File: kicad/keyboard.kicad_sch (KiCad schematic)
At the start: 64 parts

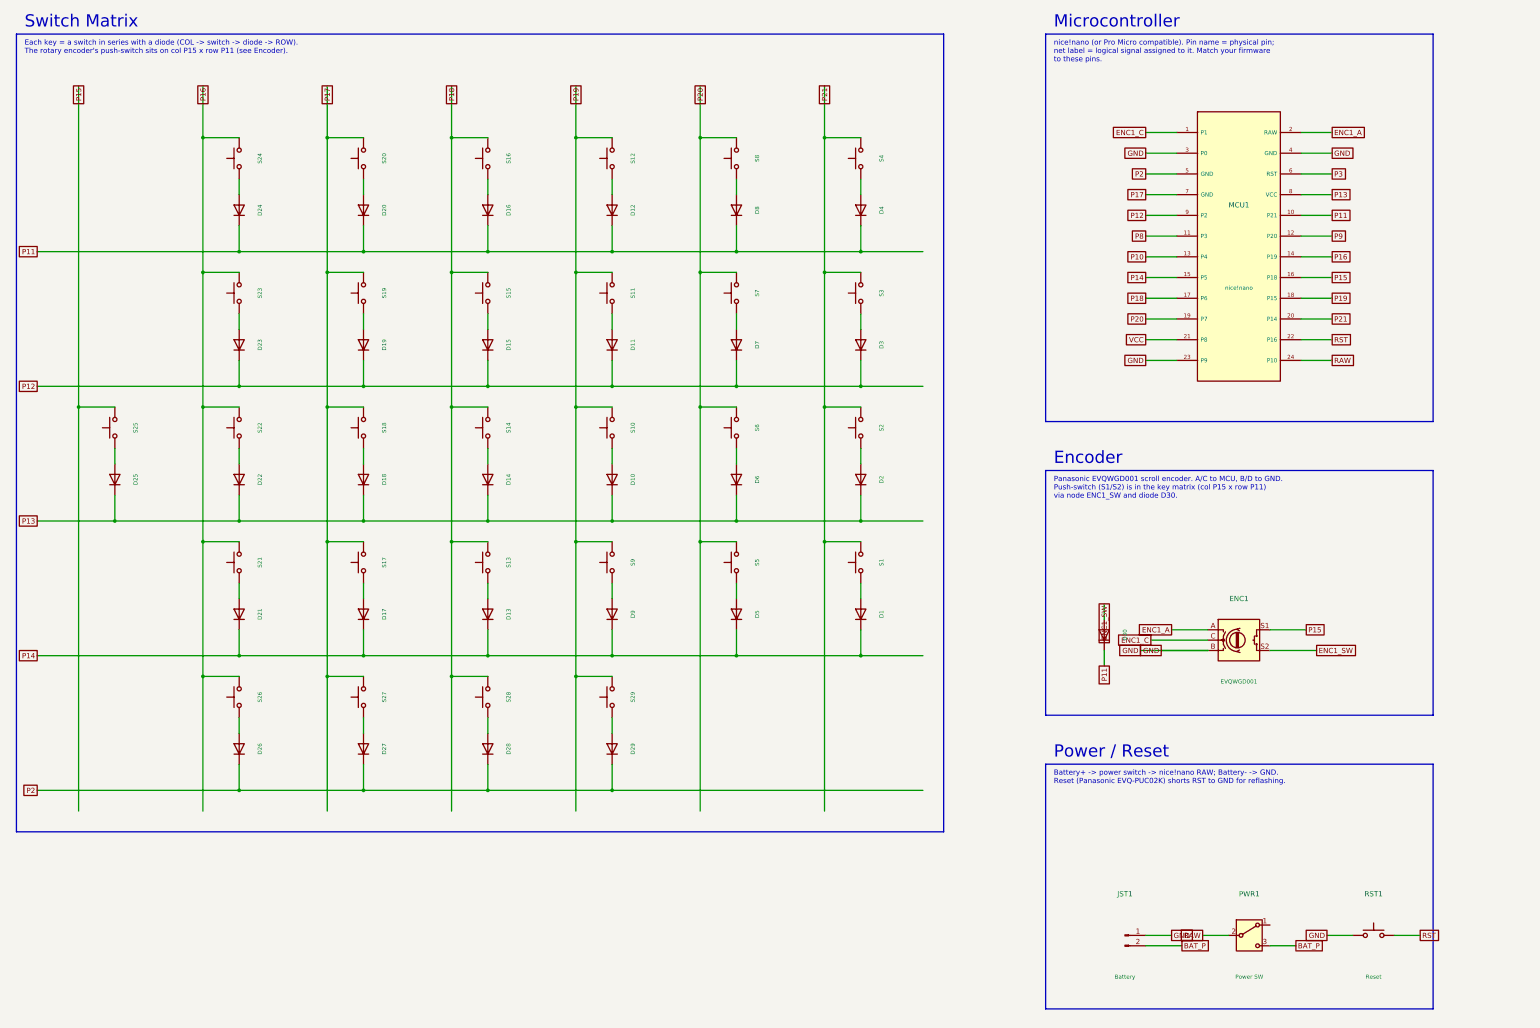
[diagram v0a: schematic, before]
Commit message: Eliminate all overlapping labels (matrix COL rails, encoder, power)
Full overlap pass driven by a bounding-box collision check (found the
overlaps my earlier point-distance check missed):
- Matrix: wider columns (33mm) and COL rail pushed further left; COL labels
  raised well above the switches with clear headroom (still attached to the
  rail top so nets resolve).
- nice!nano: pins on 5.08mm pitch so pin names + net labels never collide.
- Encoder: move the ENC1_SW diode (D30) to the far-left with its label clear;
  dedupe pins that map to the same symbol pin (B and D both GND) so GND isn't
  drawn twice at one pin.
- Power/Reset: rotate battery/switch/reset 90deg so pins fan up/down and
  reference designators sit clear of the pin labels; wider spacing.
Result: 0 label bounding-box overlaps; connectivity unchanged (54 nets).
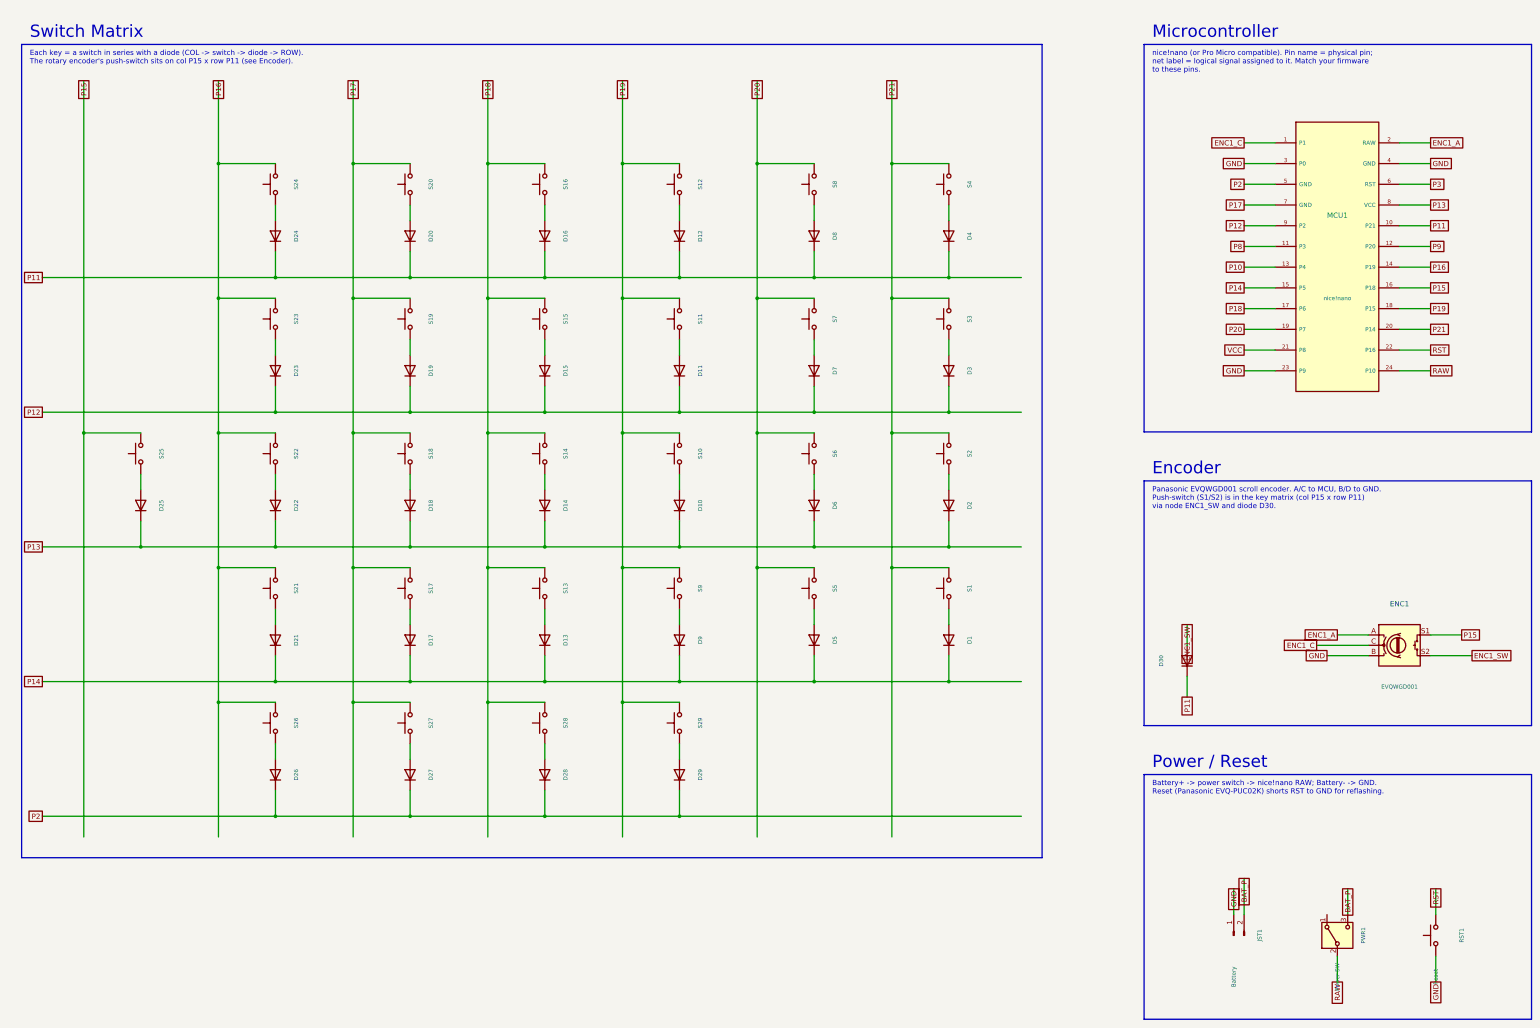
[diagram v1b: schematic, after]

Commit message: Move power/reset switches to Front; use detailed encoder WRL model
- power_switch and reset switch: side B -> F so they mount on the front
  (opposite the choc keys/hotswaps) and are accessible from that side.
- Replace crude Cosmos key-evqwgd001.step block with the detailed
  switch-evqwgd001 mesh converted to WRL. kicad-cli's raytracer does not
  render STL, so the STL was converted to VRML (coords pre-scaled by
  1/2.54 to compensate for KiCad's WRL unit factor). The encoder now
  renders as a realistic EVQWGD001 with visible roller wheel.
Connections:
- net BAT_P: now also PWR1.1 (A); no longer PWR1.3 (C)
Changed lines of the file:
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@@
       (effects (font (size 1.0 1.0))))
   )
+  (wire (pts (xy 373.38 247.65) (xy 373.38 241.30)) (stroke (width 0) (type default)))
+  (global_label "BAT_P" (shape passive) (at 373.38 241.30 90)
+    (effects (font (size 1.27 1.27)) (justify right)))
   (wire (pts (xy 375.92 257.81) (xy 375.92 264.16)) (stroke (width 0) (type default)))
   (global_label "RAW" (shape passive) (at 375.92 264.16 270)
     (effects (font (size 1.27 1.27)) (justify right)))
-  (wire (pts (xy 378.46 247.65) (xy 378.46 241.30)) (stroke (width 0) (type default)))
-  (global_label "BAT_P" (shape passive) (at 378.46 241.30 90)
-    (effects (font (size 1.27 1.27)) (justify right)))
   (symbol (lib_id "Switch:SW_Push") (at 400.05 252.73 90) (unit 1)
